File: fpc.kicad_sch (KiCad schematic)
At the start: 0 parts

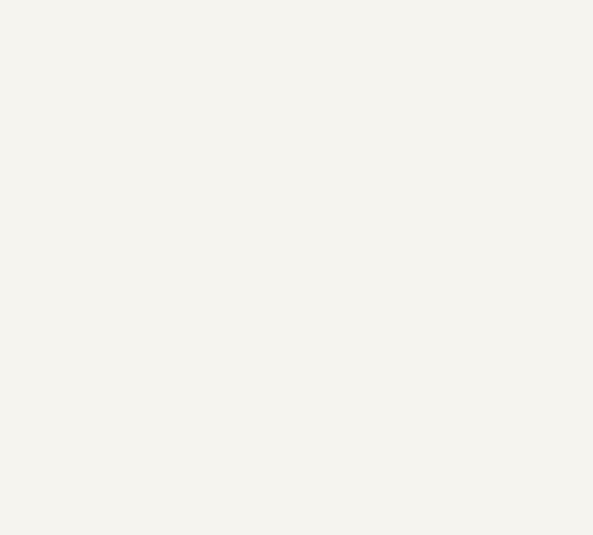
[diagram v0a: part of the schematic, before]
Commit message: Add mcu schematic
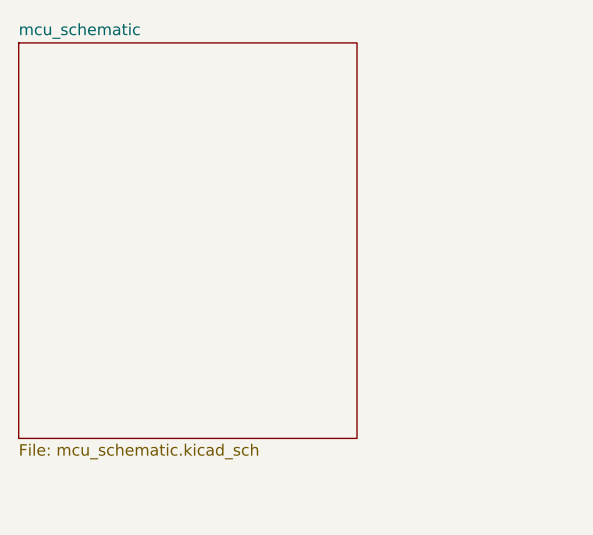
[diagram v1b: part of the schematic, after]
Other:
- added sheet mcu_schematic (mcu_schematic.kicad_sch)
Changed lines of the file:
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@@
+		)
+	)
+	(sheet
+		(at 56.515 84.328)
+		(size 37.592 43.942)
+		(exclude_from_sim no)
+		(in_bom yes)
+		(on_board yes)
+		(dnp no)
+		(fields_autoplaced yes)
+		(stroke
+			(width 0.1524)
+			(type solid)
+		)
+		(fill
+			(color 0 0 0 0.0000)
+		)
+		(property "Sheetname" "mcu_schematic"
+			(at 56.515 83.6164 0)
+			(effects
+				(font
+					(size 1.27 1.27)
+				)
+				(justify left bottom)
+			)
+		)
+		(property "Sheetfile" "mcu_schematic.kicad_sch"
+			(at 56.515 128.8546 0)
+			(effects
+				(font
+					(size 1.27 1.27)
+				)
+				(justify left top)
+			)
+		)
+		(instances
+			(project "fpc"
+				(path "/01bdb219-e962-46e0-86ef-19b214cb07d2"
+					(page "3")
+				)
+			)
 		)
 	)

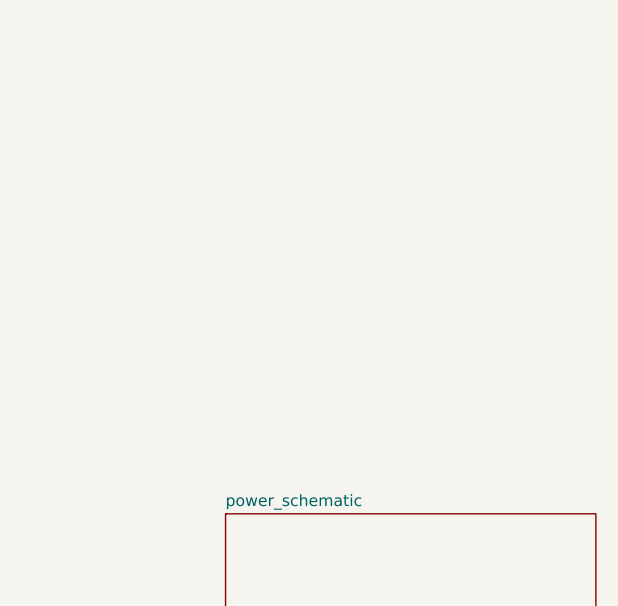
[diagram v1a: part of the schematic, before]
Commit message: relay schematic upload
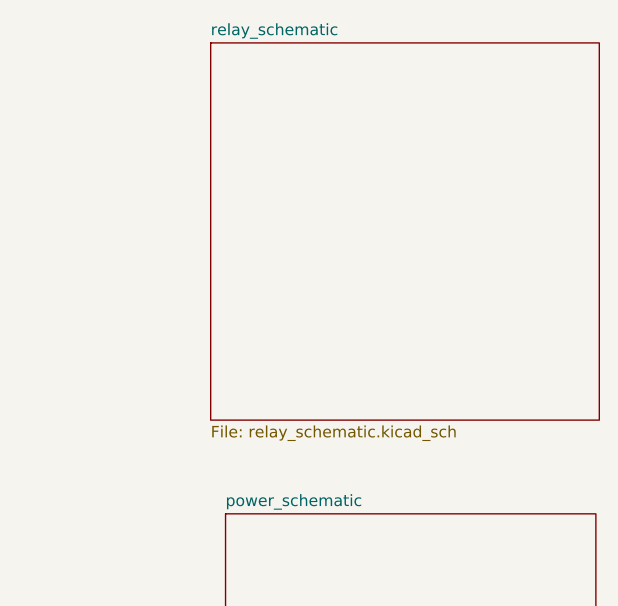
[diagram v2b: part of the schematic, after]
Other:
- added sheet relay_schematic (relay_schematic.kicad_sch)
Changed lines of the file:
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@@
+		)
+	)
+	(sheet
+		(at 212.09 36.83)
+		(size 43.18 41.91)
+		(exclude_from_sim no)
+		(in_bom yes)
+		(on_board yes)
+		(dnp no)
+		(fields_autoplaced yes)
+		(stroke
+			(width 0.1524)
+			(type solid)
+		)
+		(fill
+			(color 0 0 0 0.0000)
+		)
+		(property "Sheetname" "relay_schematic"
+			(at 212.09 36.1184 0)
+			(effects
+				(font
+					(size 1.27 1.27)
+				)
+				(justify left bottom)
+			)
+		)
+		(property "Sheetfile" "relay_schematic.kicad_sch"
+			(at 212.09 79.3246 0)
+			(effects
+				(font
+					(size 1.27 1.27)
+				)
+				(justify left top)
+			)
+		)
+		(instances
+			(project "fpc"
+				(path "/01bdb219-e962-46e0-86ef-19b214cb07d2"
+					(page "4")
+				)
+			)
 		)
 	)

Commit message: Current schematic update to main
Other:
- added sheet current_level_schematic (current_level_schematic.kicad_sch)
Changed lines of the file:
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@@
+	)
+	(sheet
+		(at 55.88 148.59)
+		(size 41.91 41.91)
+		(exclude_from_sim no)
+		(in_bom yes)
+		(on_board yes)
+		(dnp no)
+		(fields_autoplaced yes)
+		(stroke
+			(width 0.1524)
+			(type solid)
+		)
+		(fill
+			(color 0 0 0 0.0000)
+		)
+		(property "Sheetname" "current_level_schematic"
+			(at 55.88 147.8784 0)
+			(effects
+				(font
+					(size 1.27 1.27)
+				)
+				(justify left bottom)
+			)
+		)
+		(property "Sheetfile" "current_level_schematic.kicad_sch"
+			(at 55.88 191.0846 0)
+			(effects
+				(font
+					(size 1.27 1.27)
+				)
+				(justify left top)
+			)
+		)
+		(instances
+			(project "fpc"
+				(path "/01bdb219-e962-46e0-86ef-19b214cb07d2"
+					(page "5")
+				)
+			)
+		)
 	)
 	(sheet
